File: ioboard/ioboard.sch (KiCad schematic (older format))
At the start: 1 part

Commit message: Add footprints and experiment with net lists
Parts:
- added C1: C_Small, Capacitor_THT:C_Disc_D3.0mm_W1.6mm_P2.50mm, symbol Device:C_Small
- added C2, C3: 0.1uF, Capacitor_THT:C_Disc_D3.0mm_W1.6mm_P2.50mm, symbol Device:C_Small
- added U1: 74HCT245, Package_DIP:DIP-20_W7.62mm, symbol components:74HCT245
- added U2: 8086_Max_Mode, Package_DIP:DIP-40_W15.24mm, symbol MCU_Intel:8086_Max_Mode
- added U3, U5: 74LVC8T245, Package_DIP:DIP-24_W15.24mm, symbol components:74LVC8T245
- added U4, U6: 74LVC245, Package_DIP:DIP-20_W7.62mm, symbol components:74LVC245
- J1: renamed from J?; footprint (none) -> Connector_PinHeader_2.54mm:PinHeader_2x20_P2.54mm_Vertical
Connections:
- net 5V: now reaches J1.1 (VDD_5V)
- net 5V: now also C1.1, U2.40 (VCC)
- net 3.3V: now reaches J1.2 (VDD_3.3V)
- net 3.3V: now also C2.2, C3.2, U4.20 (VCC), U6.20 (VCC)
- net GND: now reaches J1.3 (GND)
- net GND: now also J1.4 (GND), C2.1, C3.1, U1.10 (GND), U4.10 (GND), U6.10 (GND)
- new net: U1.15 (B3), U2.17 (NMI)
- new net: U1.14 (B4), U2.18 (INTR)
- new net: U1.18 (B0), U2.19 (CLK)
- new net: C1.2, U2.20 (GND)
- new net: U1.16 (B2), U2.21 (RESET)
- new net: U1.17 (B1), U2.22 (READY)
- new net: U1.13 (B5), U2.23 (~TEST~)
- new net: U2.26 (~S0~), U4.2 (A0)
- new net: U2.27 (~S1~), U4.3 (A1)
- new net: U2.28 (~S2~), U4.4 (A2)
- new net: U1.12 (B6), U2.30 (~RQ~/~GT1~)
- new net: U1.11 (B7), U2.31 (~RQ~/~GT0~)
- new net: U2.35 (A19/S6), U4.8 (A6)
- new net: U2.36 (A18/S5), U4.7 (A5)
- new net: U2.37 (A17/S4), U4.6 (A4)
- new net: U2.38 (A16/S3), U4.5 (A3)
- new net: U3.11 (GND), U3.12 (GND), U3.13 (GND)
- new net: U5.11 (GND), U5.12 (GND), U5.13 (GND)
- new net ad0: U2.16 (AD0), U3.3 (A1)
- new net ad1: U2.15 (AD1), U3.4 (A2)
- new net ad10: U2.6 (AD10), U5.5 (A3)
- new net ad11: U2.5 (AD11), U5.6 (A4)
- new net ad12: U2.4 (AD12), U5.7 (A5)
- new net ad13: U2.3 (AD13), U5.8 (A6)
- new net ad14: U2.2 (AD14), U5.9 (A7)
- new net ad15: U2.39 (AD15), U5.10 (A8)
- new net ad2: U2.14 (AD2), U3.5 (A3)
- new net ad3: U2.13 (AD3), U3.6 (A4)
- new net ad4: U2.12 (AD4), U3.7 (A5)
- new net ad5: U2.11 (AD5), U3.8 (A6)
- new net ad6: U2.10 (AD6), U3.9 (A7)
- new net ad7: U2.9 (AD7), U3.10 (A8)
- new net ad8: U2.8 (AD8), U5.3 (A1)
- new net ad9: U2.7 (AD9), U5.4 (A2)
- new net n_lock: U2.29 (~LOCK~), U6.4 (A2)
- new net n_lock_3.3V: U6.16 (B2)
- new net n_rd: U2.32 (~RD~), U6.5 (A3)
- new net n_rd_3.3V: U6.15 (B3)
- new net n_s0_3.3V: U4.18 (B0)
- new net n_s1_3.3V: U4.17 (B1)
- new net n_s2_3.3V: U4.16 (B2)
- new net qs0: U2.25 (QS0), U6.2 (A0)
- new net qs0_3.3V: U6.18 (B0)
- new net qs1: U2.24 (QS1), U6.3 (A1)
- new net qs1_3.3V: U6.17 (B1)
- new net s3_3.3V: U4.15 (B3)
- new net s4_3.3V: U4.14 (B4)
- new net s5_3.3V: U4.13 (B5)
- new net s6_3.3V: U4.12 (B6)
- new net s7: U2.34 (~BHE~/S7), U4.9 (A7)
- new net s7_3.3V: U4.11 (B7)
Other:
- moved on the sheet: J1

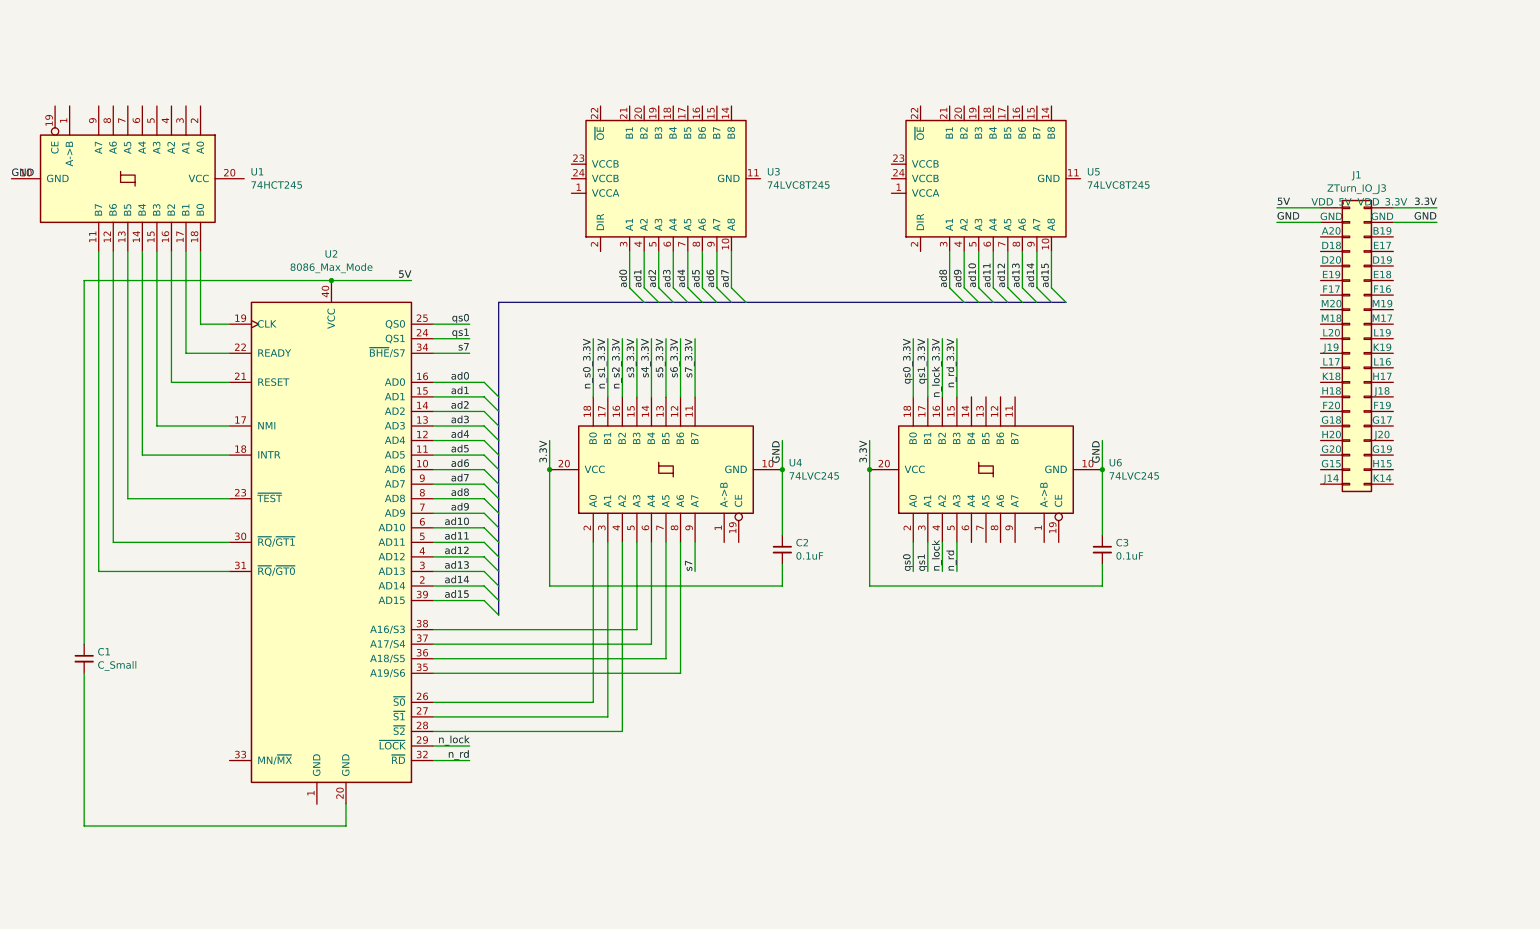
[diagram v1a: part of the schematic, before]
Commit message: Rework IO board design
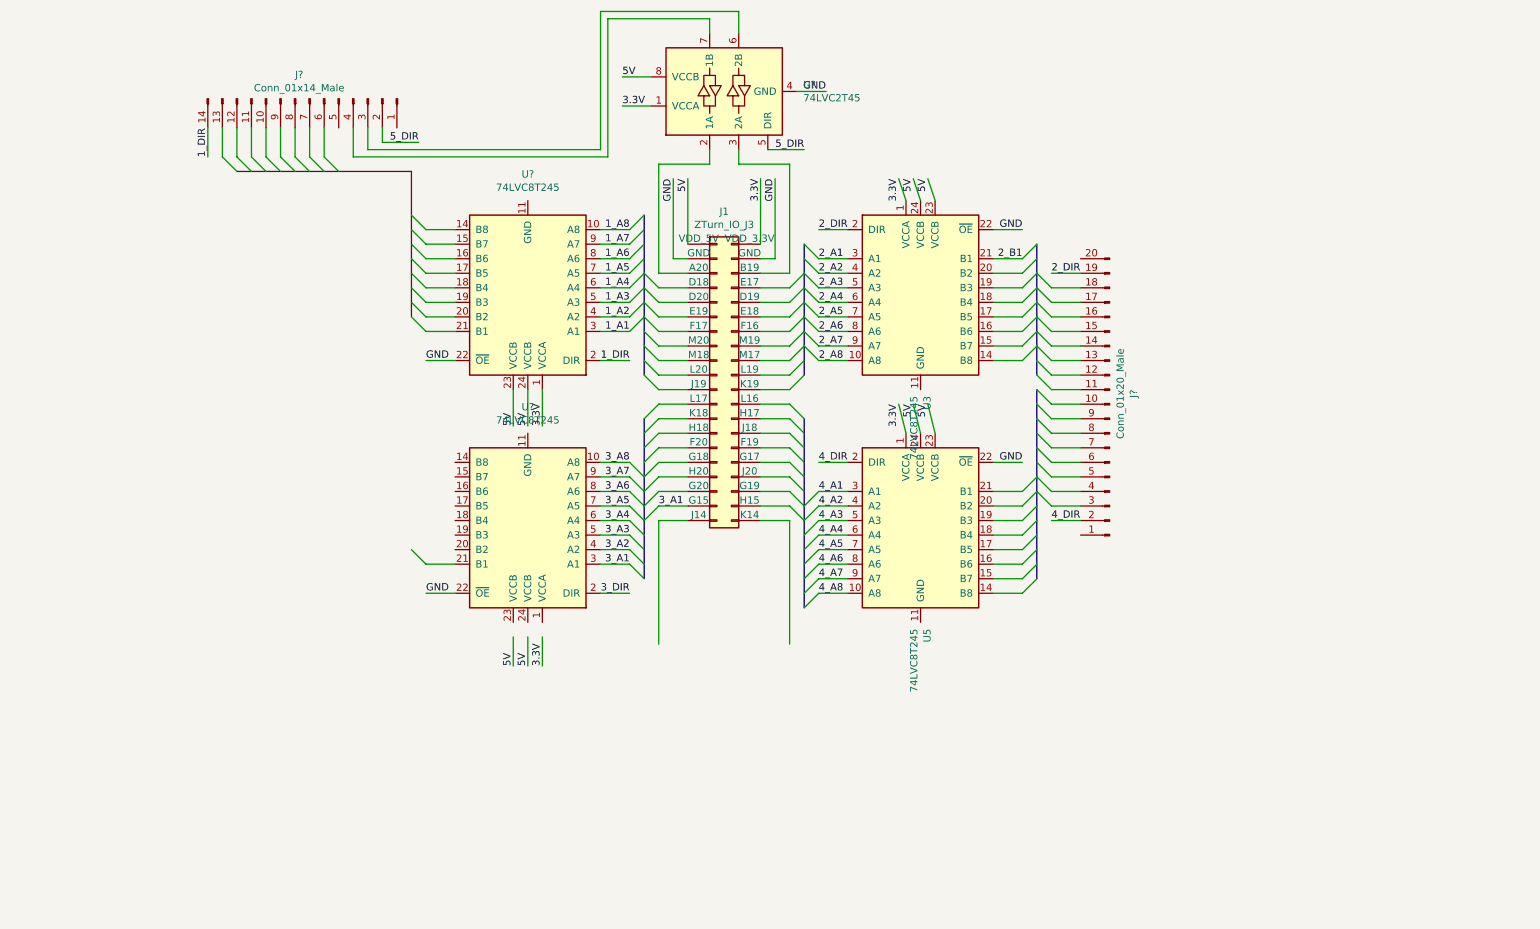
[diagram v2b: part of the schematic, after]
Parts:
- removed C1: C_Small, Capacitor_THT:C_Disc_D3.0mm_W1.6mm_P2.50mm, symbol Device:C_Small
- removed C2, C3: 0.1uF, Capacitor_THT:C_Disc_D3.0mm_W1.6mm_P2.50mm, symbol Device:C_Small
- removed U1: 74HCT245, Package_DIP:DIP-20_W7.62mm, symbol components:74HCT245
- removed U2: 8086_Max_Mode, Package_DIP:DIP-40_W15.24mm, symbol MCU_Intel:8086_Max_Mode
- removed U4, U6: 74LVC245, Package_DIP:DIP-20_W7.62mm, symbol components:74LVC245
- added J?: Conn_01x20_Male, symbol Connector:Conn_01x20_Male
- added J?: Conn_01x14_Male, symbol Connector:Conn_01x14_Male
- added U? (x2): 74LVC8T245, symbol components:74LVC8T245
- added U?: 74LVC2T45, symbol components:74LVC2T45
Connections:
- net 3.3V: now also U3.1 (VCCA), U5.1 (VCCA), U?.1 (VCCA), U?.1 (VCCA)
- net 5V: now also U3.23 (VCCB), U3.24 (VCCB), U5.23 (VCCB), U5.24 (VCCB), U?.23 (VCCB), U?.24 (VCCB), U?.8 (VCCB)
- net GND: now also U3.22 (~OE), U5.22 (~OE), U?.22 (~OE), U?.22 (~OE), U?.4 (GND)
- net 3_A1: now reaches J1.37 (G15)
- net 3_A1: now also U?.3 (A1)
- net at J1.5 (A20): now also U?.2 (1A)
- net at J1.6 (B19): now also U?.3 (2A)
- net 2_DIR: now reaches U3.2 (DIR)
- net 2_DIR: now also J?.19 (Pin_19)
- net 2_B1: now reaches U3.21 (B1)
- net 4_DIR: now reaches U5.2 (DIR)
- net 4_DIR: now also J?.2 (Pin_2)
- net ad0 renamed 2_A1
- net ad1 renamed 2_A2
- net ad10 renamed 4_A3
- net ad11 renamed 4_A4
- net ad12 renamed 4_A5
- net ad13 renamed 4_A6
- net ad14 renamed 4_A7
- net ad15 renamed 4_A8
- net ad2 renamed 2_A3
- net ad3 renamed 2_A4
- net ad4 renamed 2_A5
- net ad5 renamed 2_A6
- net ad6 renamed 2_A7
- net ad7 renamed 2_A8
- net ad8 renamed 4_A1
- net ad9 renamed 4_A2
- new net: U?.11 (GND), U?.12 (GND), U?.13 (GND) (x2)
- new net: J?.3 (Pin_3), U?.6 (2B)
- new net: J?.4 (Pin_4), U?.7 (1B)
- new net 1_A1: U?.3 (A1)
- new net 1_A2: U?.4 (A2)
- new net 1_A3: U?.5 (A3)
- new net 1_A4: U?.6 (A4)
- new net 1_A5: U?.7 (A5)
- new net 1_A6: U?.8 (A6)
- new net 1_A7: U?.9 (A7)
- new net 1_A8: U?.10 (A8)
- new net 1_DIR: J?.14 (Pin_14), U?.2 (DIR)
- new net 3_A2: U?.4 (A2)
- new net 3_A3: U?.5 (A3)
- new net 3_A4: U?.6 (A4)
- new net 3_A5: U?.7 (A5)
- new net 3_A6: U?.8 (A6)
- new net 3_A7: U?.9 (A7)
- new net 3_A8: U?.10 (A8)
- new net 3_DIR: U?.2 (DIR)
- new net 5_DIR: J?.2 (Pin_2), U?.5 (DIR)
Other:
- moved on the sheet: J1, U3, U5
